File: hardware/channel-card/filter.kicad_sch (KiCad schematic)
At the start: 110 parts, among them J181 CUTOFF CV 1 V/oct, SW181 FILTER BYPASS (latching), U101 SSI2144, U102 SSI2144, U103 LM13700, U104 NE5532, U105 NE5532, U106 NE5532, U107 NE5532, U108 DG413DY

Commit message: Channel card: meter LEDs 0805, op amp power levers (decision 123), RoHS audit
- Meter D411-D418 to 0805 LEDs (KT-0805G, KT-0805Y, NCD0805R1; decision 119)
- U107 NE5532 -> TL072; meter U401/U404 TL072 -> TL062CDR (SX-IC-024)
- Card load 113 / 95 mA typical, sizing 174 / 142 mA; netlists match, ERC 0/0
- RoHS audit of parts.csv (decision 122): 47 rows sourced; gaps SSI2144,
  SSI2162, AS3046D; THAT1646S08-U and ERA-V33J102V end of life at Mouser
  (docs/reviews/2026-10-09-rohs-audit.md); four rows requoted

Co-Authored-By: Claude Opus 5.5 <noreply@anthropic.com>
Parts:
- removed U107: NE5532, Package_SO:SOIC-8_3.9x4.9mm_P1.27mm, symbol Amplifier_Operational:NE5532
- added U107: TL072, Package_SO:SOIC-8_3.9x4.9mm_P1.27mm, symbol Amplifier_Operational:TL072
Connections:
- net +15V: now also U107.8 (V+)
- net -15V: now also U107.4 (V-)
- net AGND: now also U107.3 (+), U107.5 (+)
- net FCV: now also U107.1
- net at C181.1, R181.2, R182.2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: now also U107.2 (-)
- new net: U107.6 (-), U107.7

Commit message: Channel card: pot MPNs on the symbols, R184 12k for the RESONANCE pot rating (decision 129)
- Alpha MPNs on RV1 (TRIM), RV181 (CUTOFF), RV301/RV302 (AUX); the Thonk
  -0057 variant suffix is left open
- RV183 reference netlist now SX-POT-012 (Tayda RD901F-40-15K-C10K),
  matching the drawing
- Decision 129: Alpha's RD901F spec rates non-B tapers at 0.02 W; RV183
  carried about 21 mW, R184 10k -> 12k gives about 17 mW (max Q current
  about 254 uA, provisional with R120/R170)
- RD901F spec facts in parts.csv; master STATUS notes RV402 RELEASE at
  about 20.2 mW for its own session

Netlists match, ERC 0/0.

Co-Authored-By: Claude Opus 5.5 <noreply@anthropic.com>
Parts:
- R184: value 10k -> 12k; Note (none) -> R184 12k keeps RV183 within Alpha's 0.02 W non-B rating (17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; ProjectPN SX-R-002 -> SX-R-008
- RV181: MPN (none) -> RD901F-40-15K-B50K-0057

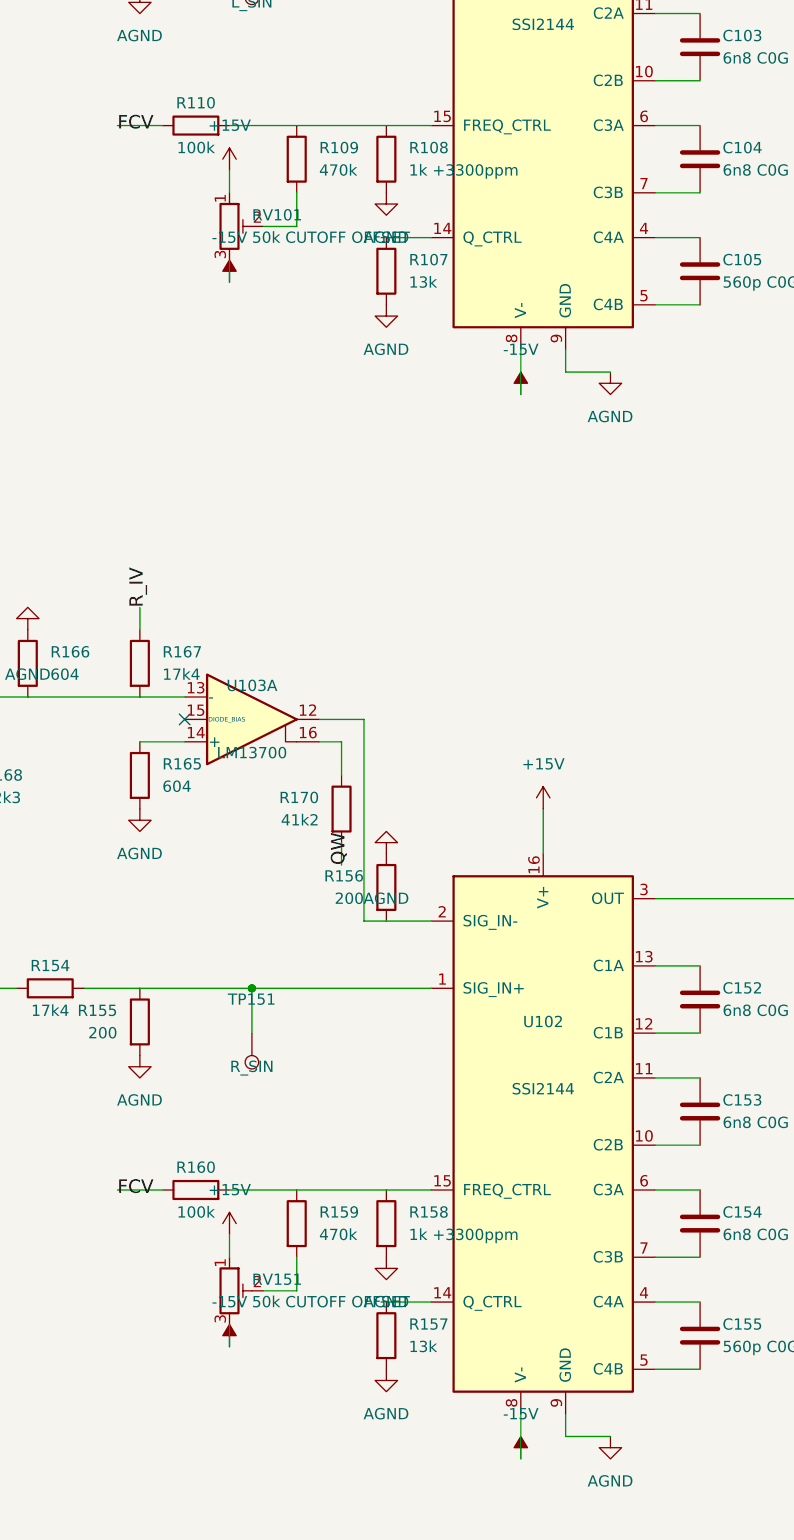
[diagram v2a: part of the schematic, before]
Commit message: Channel card: TFPT tempco pair replaces the end-of-life ERA-V33J102V (decision 130)
- R108/R158 Vishay TFPT0603L8200FV 820R (+4110 ppm/K) with new R122/R172
  180R in series to AGND: 1k at about +3370 ppm/K, divider unchanged
- SX-R-089, SX-R-090 in parts.csv; SX-R-021 stays for master R421
- Trim pot value text shortened to "50k OFFSET" for room on the sheet
- STATUS, handoff, hardware notes (datasheet routes, pot power rating);
  master STATUS points R421 at the same pair

Netlists match, ERC 0/0, reuse lint clean.

Co-Authored-By: Claude Opus 5.5 <noreply@anthropic.com>
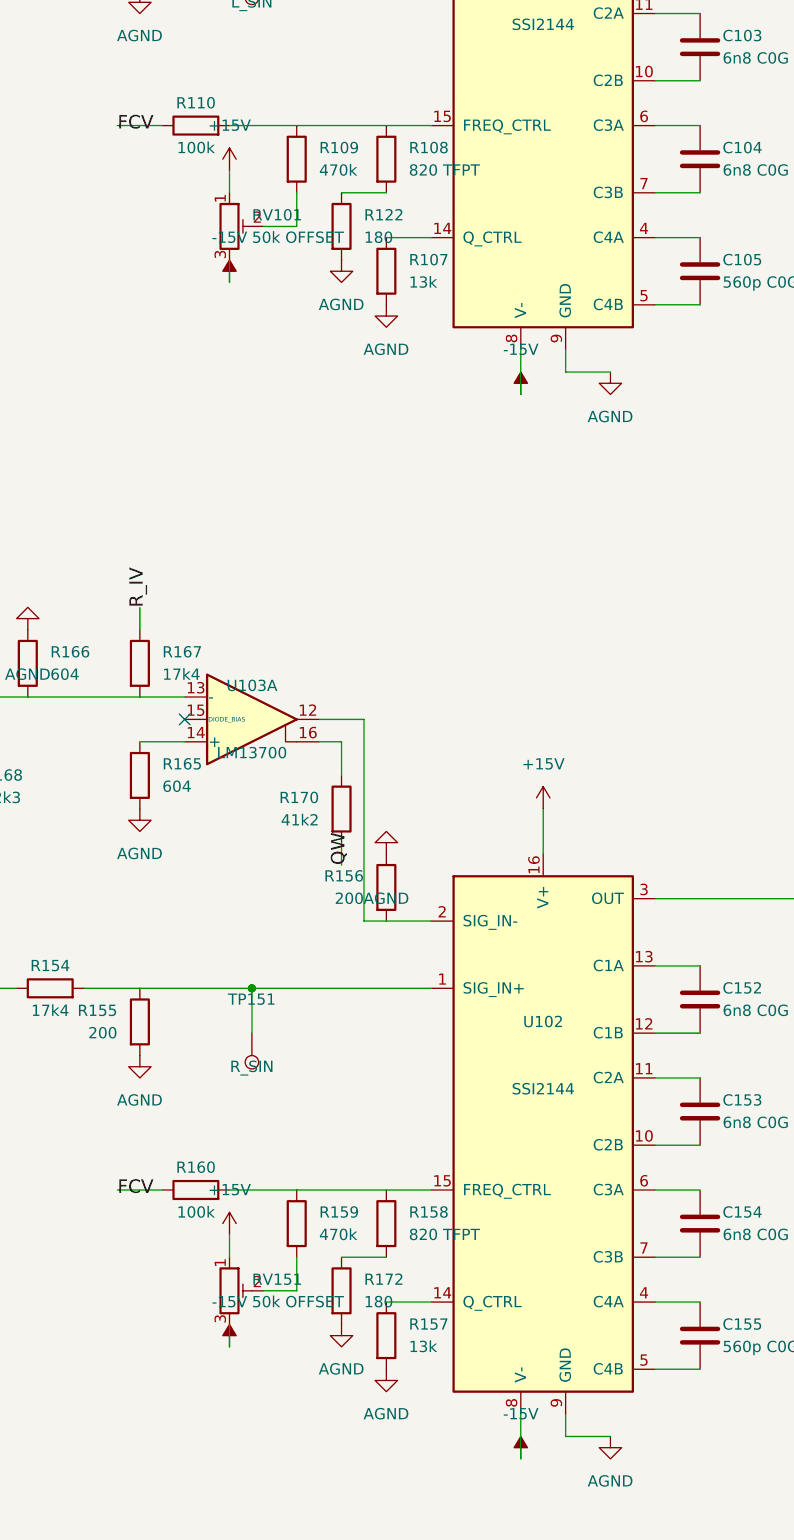
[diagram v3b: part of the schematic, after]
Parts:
- added R122, R172: 180, Resistor_SMD:R_0805_2012Metric, symbol Device:R
- R108, R158: value 1k +3300ppm -> 820 TFPT; MPN ERA-V33J102V -> TFPT0603L8200FV; Manufacturer Panasonic -> Vishay; Note Temperature-compensating; place against the SSI2144 -> Vishay TFPT linear PTC thin film, +4110 ppm/K; in series wi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; ProjectPN SX-R-021 -> SX-R-089; Supplier (none) -> Mouser; SupplierPN (none) -> 71-TFPT0603L8200FV
- RV101, RV151: value 50k CUTOFF OFFSET -> 50k OFFSET
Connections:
- net AGND: now also R122.2, R172.2; no longer R108.2, R158.2
- new net: R158.2, R172.1
- new net: R108.2, R122.1

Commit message: Channel card: fee-free TL072CDT, 78L05G-AB3-R, BZT52C6V2, UNI-ROYAL resistors (decision 137)
SX-IC-007 TL072 -> ST TL072CDT (LCSC C6961, basic), SX-IC-012 78L05 -> UTC
78L05G-AB3-R (C71136, basic; pins 1 O 2 G 3 I, not the -AB3-C-R variant),
SX-D-001 -> hongjiacheng BZT52C6V2 (C19077403, preferred), SX-R-011/036/042
-> UNI-ROYAL 0805W8F (preferred). Datasheet facts and RoHS sources in
parts.csv. Filter, level, meter and chain sheets rebuilt: netlists match,
ERC 0/0. costs.py extended: 82 -> 80 fee types. Master STATUS notes that
its TL072 symbols still need the ST fields.

Co-Authored-By: Claude Opus 5.5 <noreply@anthropic.com>
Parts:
- U107: MPN (none) -> TL072CDT; Manufacturer Texas Instruments -> STMicroelectronics; Supplier (none) -> LCSC; SupplierPN (none) -> C6961

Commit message: Channel card: cost levers (decisions 139-143)
- U303 DG412 -> DG413, SC send on the NC section (139)
- All values E24 with JLCPCB fee-free parts; E24 pairs for V/oct
  and fader law, meter ladder re-fitted (140)
- Filter temperature compensation to the backlog (141)
- MUTE/DUCK switched by the buttons' spare pole, U206 DG413 removed;
  100k hold resistors, no dependence on contact sequence (142)
- TL072 difference receiver with 10k 0.1 % instead of the AD8273 (143)
- Trimmers from Mouser, CUTOFF pot from Tayda A-4730
- Breadboard tests 11 (X5R coupling caps) and 12 (fixed V/oct)
- costs.py estimate, 4 channels: EUR 1,035 -> 946

Co-Authored-By: Claude Opus 5.5 <noreply@anthropic.com>
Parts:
- added R187: 12k, Resistor_SMD:R_0805_2012Metric, symbol Device:R
- R103, R153: value 16k9 -> 16k; ProjectPN SX-R-017 -> SX-R-005
- R104, R117, R119, R154, R167, R169: value 17k4 -> 18k; ProjectPN SX-R-009 -> SX-R-092
- R108, R158: value 820 TFPT -> 820; footprint Resistor_SMD:R_0603_1608Metric -> Resistor_SMD:R_0805_2012Metric; MPN TFPT0603L8200FV -> (none); Manufacturer Vishay -> (none); Note Vishay TFPT linear PTC thin film, +4110 ppm/K; in series wi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 -> Plain 820R: temperature compensation moved to the backlog (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; ProjectPN SX-R-089 -> SX-R-100; Supplier Mouser -> (none); SupplierPN 71-TFPT0603L8200FV -> (none)
- R111, R161: value 8k66 -> 9k1; ProjectPN SX-R-014 -> SX-R-095
- R113, R163: value 6k04 -> 6k2; ProjectPN SX-R-016 -> SX-R-091
- R115, R116, R165, R166: value 604 -> 560; ProjectPN SX-R-012 -> SX-R-094
- R118, R168: value 52k3 -> 51k; ProjectPN SX-R-013 -> SX-R-093
- R120, R170: value 41k2 -> 36k; ProjectPN SX-R-015 -> SX-R-097
- R122, R172: Note Low-tempco part of the 1k tempco leg (decision 130); keep t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 -> With R108/R158 820R = 1k FREQ leg (decision 141)
- R181: value 301k -> 300k; ProjectPN SX-R-018 -> SX-R-096
- R183: value 162k -> 150k; ProjectPN SX-R-019 -> SX-R-098
- RV101, RV151, RV182: Supplier (none) -> Mouser; SupplierPN (none) -> 652-3296W-1-503LF
- RV181: MPN RD901F-40-15K-B50K-0057 -> RD901F-40-15K-B50K; Supplier Thonk -> Tayda; SupplierPN (none) -> A-4730
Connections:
- net at R183.2: now also R187.1; no longer RV182.1
- new net: R187.2, RV182.1

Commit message: Channel card: R217 30k (decision 153), SSI2144/SSI2162 hand-soldered on the prototype (decision 155)
Level sheet: R217 30k1 -> 30k (SX-R-050, basic); ducking -10.10 dB per -1 V
in simulation/level. U101/U102 SSI2144 and U201 SSI2162 carry Assembly =
"hand (decision 155)": 38 -> 36 fee types, 4/8/16 channels EUR 788/1,069/1,665.
Bipolar 10 uF caps stay consigned until breadboard test 11. Netlists match,
ERC 0/0.

Co-Authored-By: Claude Opus 5.5 <noreply@anthropic.com>
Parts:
- U101, U102: Assembly (none) -> hand (decision 155)

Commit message: Buttons: SX-SW-001 is the latching GPBS850L, not the momentary GPBS850N
Electrokit 41012905 (on-on, latching) links the GPBS850N datasheet, which
is the momentary twin (Electrokit 41015527, Mouser "Non-Latching ON-(ON)");
the MPN was copied from that file. The latching part is CW GPBS850L
(datasheet Rev 2, 2014: same body, pin grid and pressed = 2-3, 5-6 contacts;
plunger 4.0 mm instead of 3.8).

MPN and footprint name corrected on all 17 button symbols, the generator
scripts and the input reference; parts.csv gets the GPBS850L datasheet and
RoHS source (Mouser 629-GPBS-850L, DigiKey CW179-ND); prices.csv gets the
Electrokit price (6.48 SEK ex VAT at 25+). Erratum on decision 75, checklist
item for the delivered switches and cap sizing, correction notes in the
RoHS audit and the cost review. No wiring change; ERC 0/0 on both cards.
Estimate €769 / €1,037 / €1,609 for 4 / 8 / 16 channels.

Co-Authored-By: Claude Opus 5.5 <noreply@anthropic.com>
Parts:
- SW181: footprint syntsamix:SW_Latching_8.5x8.5mm_CW_GPBS850N -> syntsamix:SW_Latching_8.5x8.5mm_CW_GPBS850L; MPN GPBS850N -> GPBS850L
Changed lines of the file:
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@@
 			)
 		)
-		(property "Footprint" "syntsamix:SW_Latching_8.5x8.5mm_CW_GPBS850N"
+		(property "Footprint" "syntsamix:SW_Latching_8.5x8.5mm_CW_GPBS850L"
 			(at 185.42 299.72 0)
 			(hide yes)
@@
 			)
 		)
-		(property "MPN" "GPBS850N"
+		(property "MPN" "GPBS850L"
 			(at 185.42 299.72 0)
 			(hide yes)

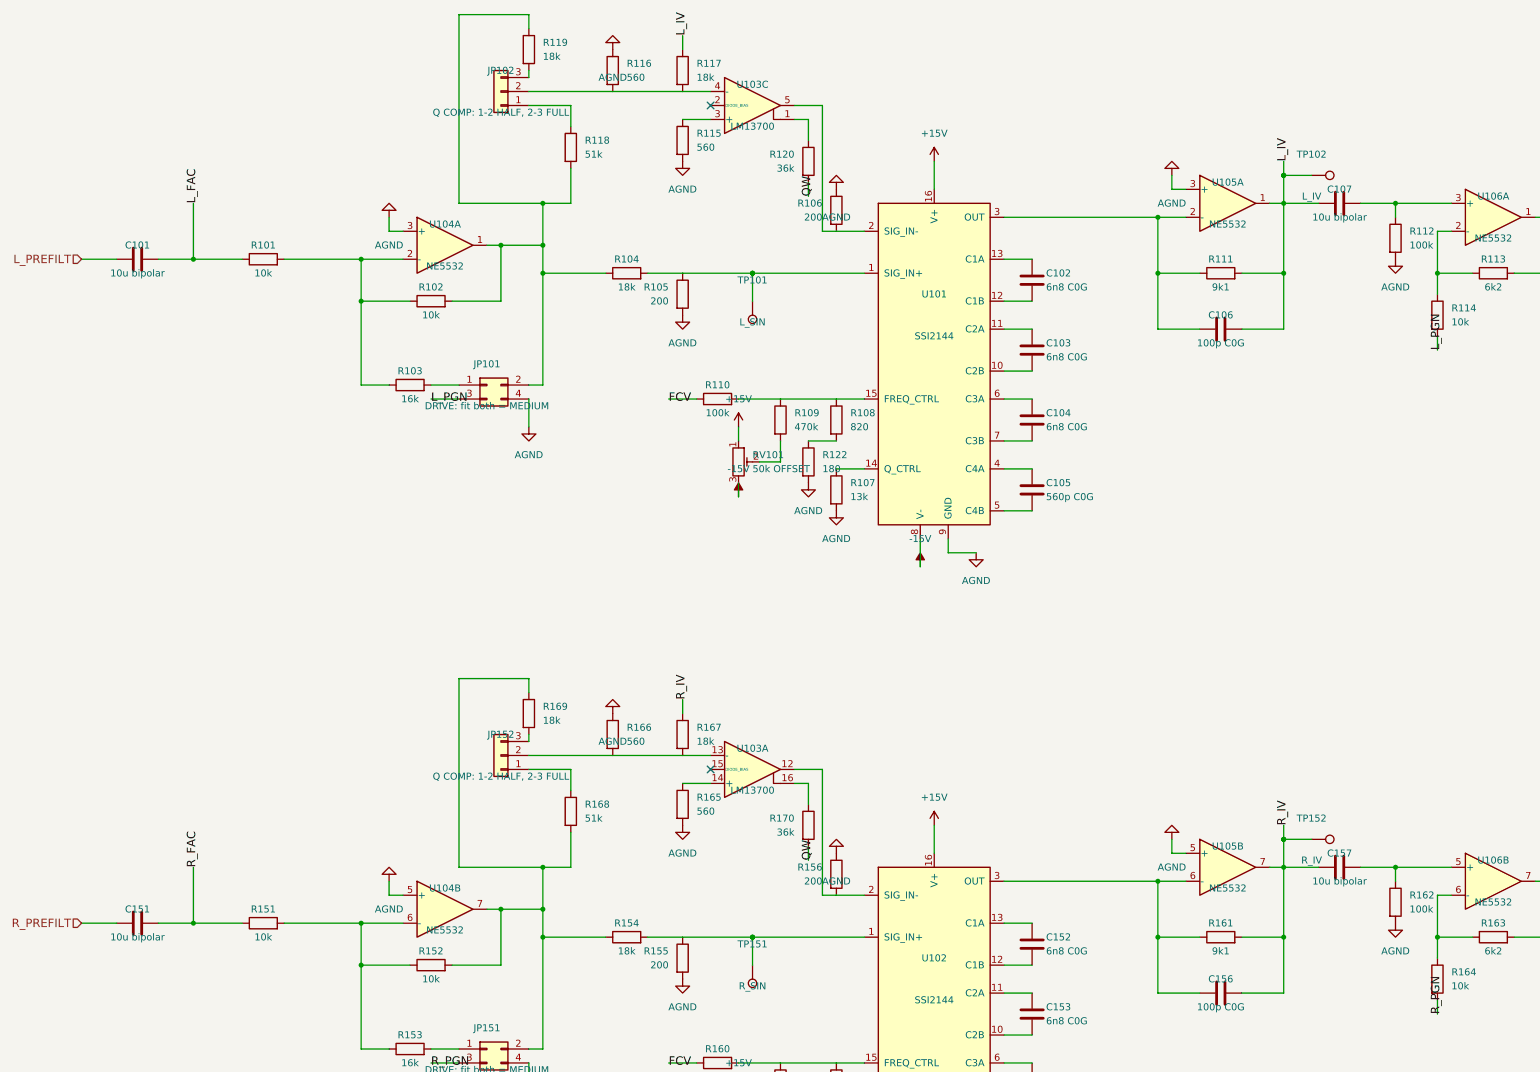
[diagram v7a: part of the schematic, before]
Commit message: Channel card: coupling capacitors as back-to-back ROQANG pairs (decision 161)
Each 10 uF bipolar coupling capacitor (Panasonic EEE-1VA100NP, out of stock
at LCSC and consigned) becomes two ROQANG RVT1V100M0505 10 uF 35 V (SX-C-024,
already on the card) in series, negative to negative: C5+C21, C6+C22,
C101+C108, C151+C158, C107+C109, C157+C159, C221+C235, C271+C285. No new fee
type, nothing on the channel card consigned. Netlists match (input 48,
filter 85, level 43 nets), ERC 0/0. Breadboard test 11 now checks the pair;
the X5R option is dropped. Estimate EUR 778 -> 768 for 4 channels; the
master follows in its own session.

Co-Authored-By: Claude Opus 5.5 <noreply@anthropic.com>
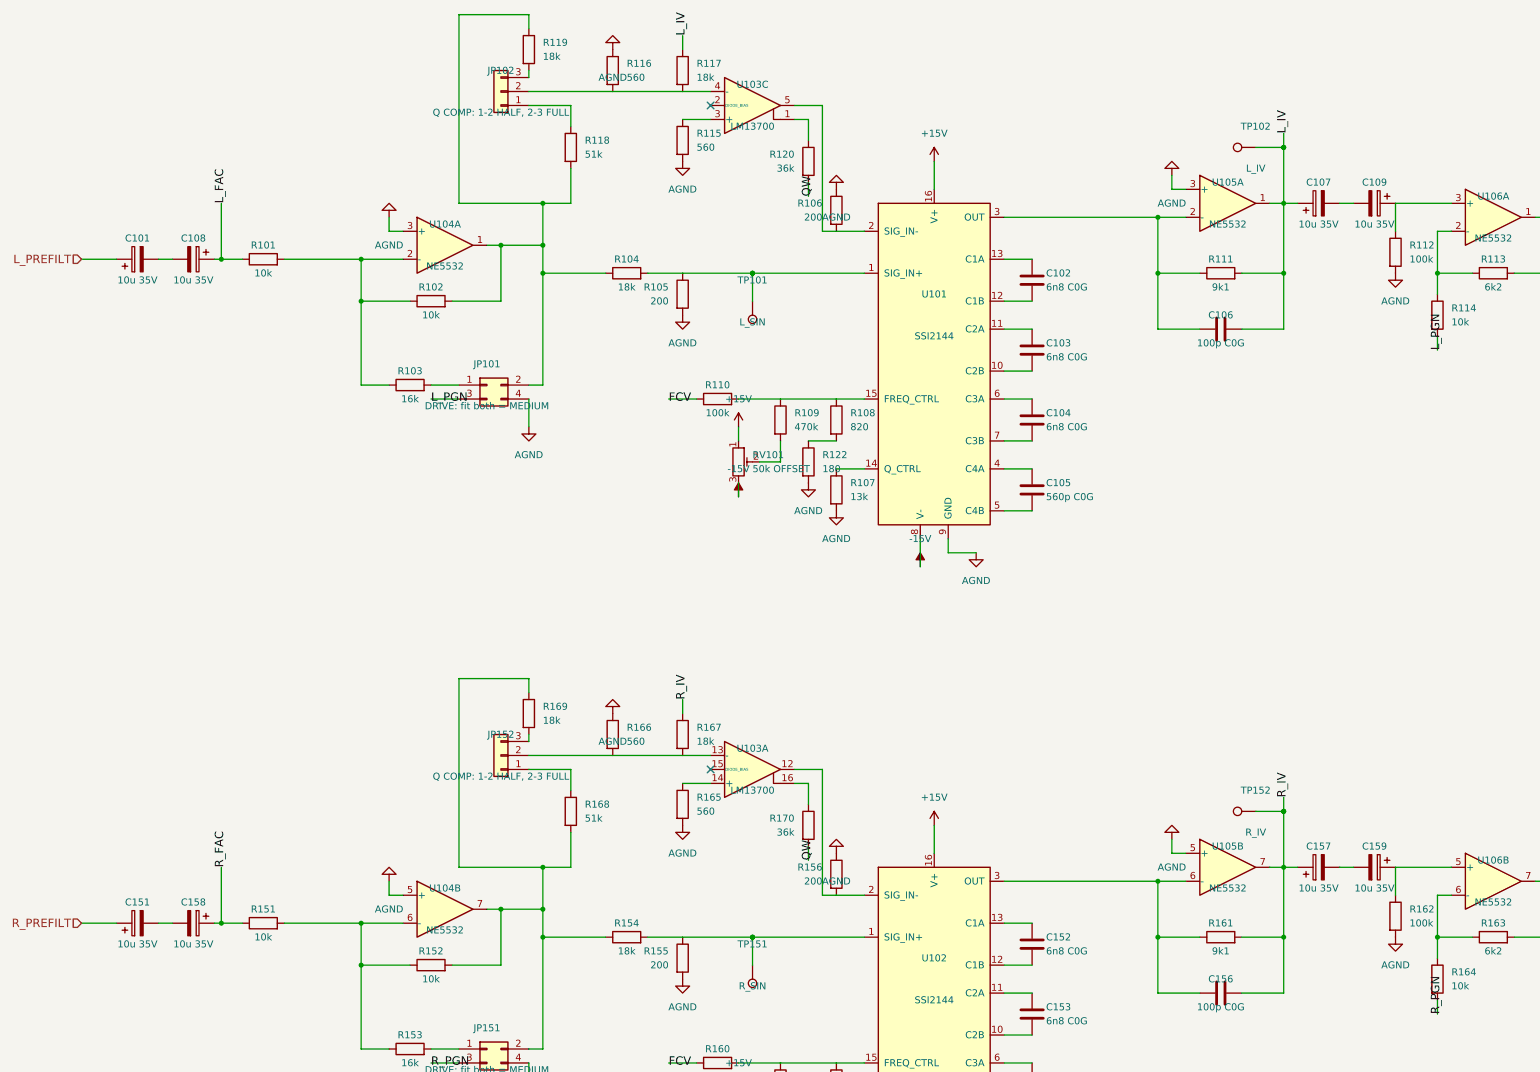
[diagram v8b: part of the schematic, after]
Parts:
- removed C101, C107, C151, C157: 10u bipolar, Capacitor_SMD:C_Elec_6.3x5.4, symbol Device:C
- added C101, C107, C108, C109, C151, C157, C158, C159: 10u 35V, Capacitor_SMD:CP_Elec_5x5.4, symbol Device:C_Polarized
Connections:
- net L_FAC: now also C108.1
- net L_IV: now also C107.1
- net L_PREFILT: now also C101.1
- net R_FAC: now also C158.1
- net R_IV: now also C157.1
- net R_PREFILT: now also C151.1
- net at R162.1, U106.5 (+): now also C159.1
- net at R112.1, U106.3 (+): now also C109.1
- new net: C151.2, C158.2
- new net: C157.2, C159.2
- new net: C107.2, C109.2
- new net: C101.2, C108.2
